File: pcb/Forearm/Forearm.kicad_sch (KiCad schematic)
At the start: 9 parts, among them J1 Conn_01x08_IMU_0, J2 Conn_01x16_Ribbon_To_Top, J3 Conn_01x16_Ribbon_To_Bottom, J4 Conn_01x03_DFR0205, U1 ESP32-S3-DEVKITC-1-N8R2

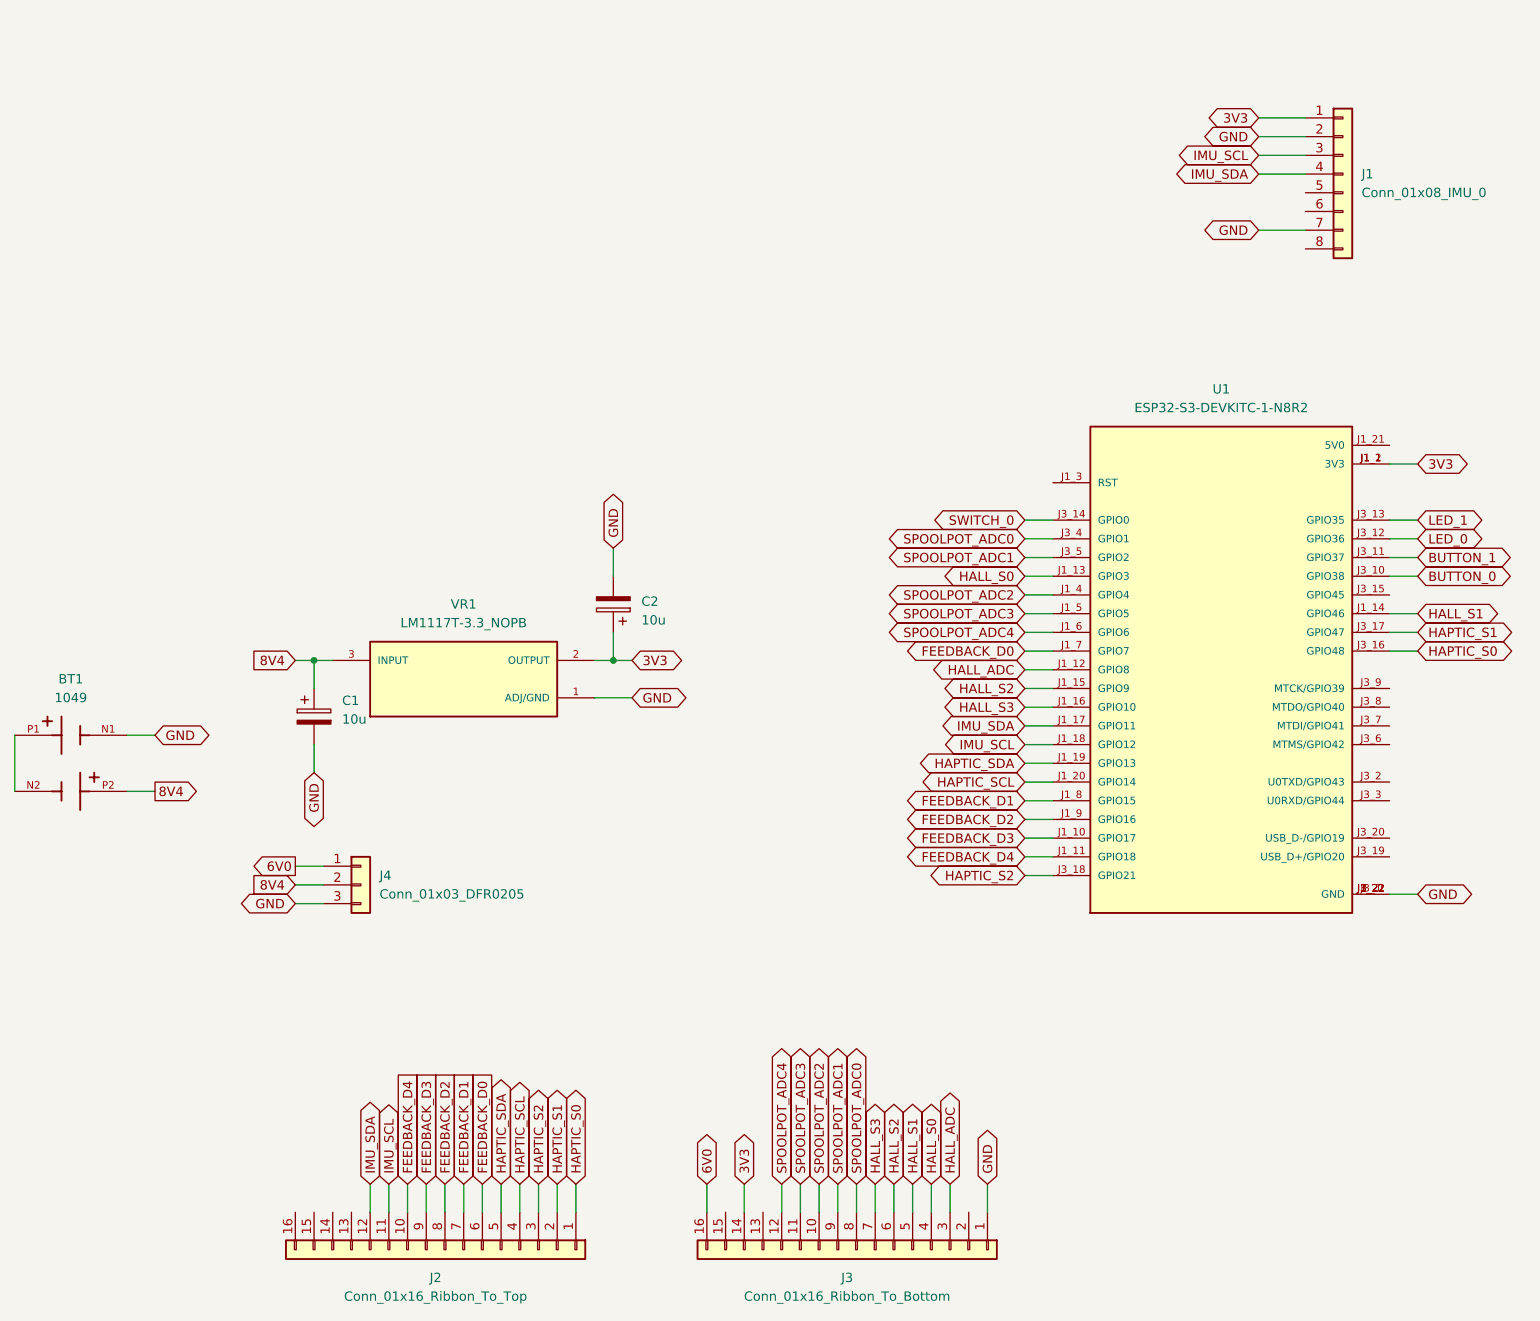
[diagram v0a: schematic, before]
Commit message: forward annotated schms to pcbs, added gnd and pwr planes, begun part placement
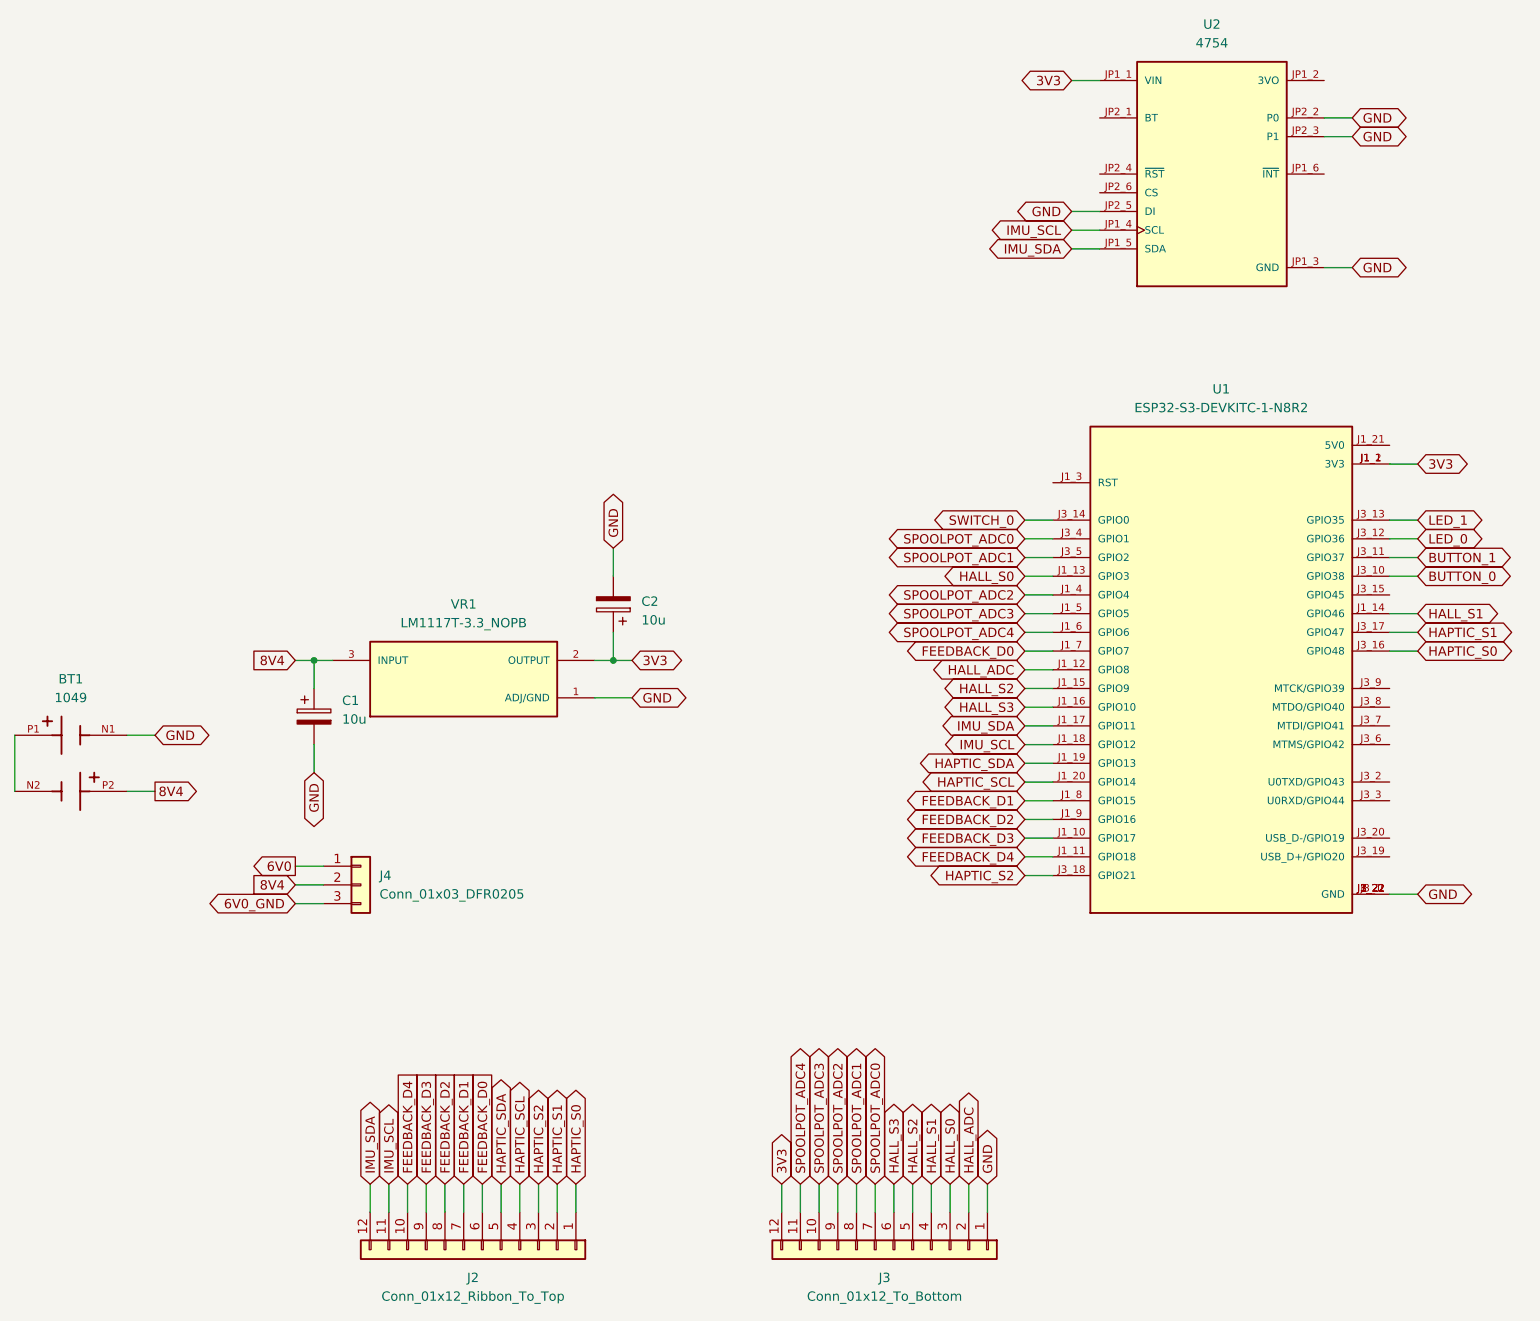
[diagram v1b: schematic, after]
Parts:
- removed J1: Conn_01x08_IMU_0, symbol Connector_Generic:Conn_01x08
- removed J2: Conn_01x16_Ribbon_To_Top, symbol Connector_Generic:Conn_01x16
- removed J3: Conn_01x16_Ribbon_To_Bottom, symbol Connector_Generic:Conn_01x16
- added J2: Conn_01x12_Ribbon_To_Top, 0522071233:0522071233, symbol Connector_Generic:Conn_01x12
- added J3: Conn_01x12_To_Bottom, 0522071233:0522071233, symbol Connector_Generic:Conn_01x12
- added U2: 4754, BNO085:MODULE_4754, symbol BNO085:4754
- C1, C2: footprint (none) -> Capacitor_THT:CP_Radial_Tantal_D6.0mm_P2.50mm
- J4: footprint (none) -> DFR0205:DFR0205
- VR1: footprint LM1117T-3.3_NOPB:TO254P1054X470X1955-3 -> LM1117T-3.3:LM1117T-3.3_NOPB
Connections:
- net 3V3: now also J3.12 (Pin_12), U2.JP1_1 (VIN)
- net FEEDBACK_D0: now also J2.6 (Pin_6)
- net FEEDBACK_D1: now also J2.7 (Pin_7)
- net FEEDBACK_D2: now also J2.8 (Pin_8)
- net FEEDBACK_D3: now also J2.9 (Pin_9)
- net FEEDBACK_D4: now also J2.10 (Pin_10)
- net GND: now also J3.1 (Pin_1), U2.JP1_3 (GND), U2.JP2_2 (P0), U2.JP2_3 (P1), U2.JP2_5 (DI); no longer J4.3 (Pin_3)
- net HALL_ADC: now also J3.2 (Pin_2)
- net HALL_S0: now also J3.3 (Pin_3)
- net HALL_S1: now also J3.4 (Pin_4)
- net HALL_S2: now also J3.5 (Pin_5)
- net HALL_S3: now also J3.6 (Pin_6)
- net HAPTIC_S0: now also J2.1 (Pin_1)
- net HAPTIC_S1: now also J2.2 (Pin_2)
- net HAPTIC_S2: now also J2.3 (Pin_3)
- net HAPTIC_SCL: now also J2.4 (Pin_4)
- net HAPTIC_SDA: now also J2.5 (Pin_5)
- net IMU_SCL: now also J2.11 (Pin_11), U2.JP1_4 (SCL)
- net IMU_SDA: now also J2.12 (Pin_12), U2.JP1_5 (SDA)
- net SPOOLPOT_ADC0: now also J3.7 (Pin_7)
- net SPOOLPOT_ADC1: now also J3.8 (Pin_8)
- net SPOOLPOT_ADC2: now also J3.9 (Pin_9)
- net SPOOLPOT_ADC3: now also J3.10 (Pin_10)
- net SPOOLPOT_ADC4: now also J3.11 (Pin_11)
- new net 6V0_GND: J4.3 (Pin_3)

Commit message: revised hand and made pass at routing forearm pcb
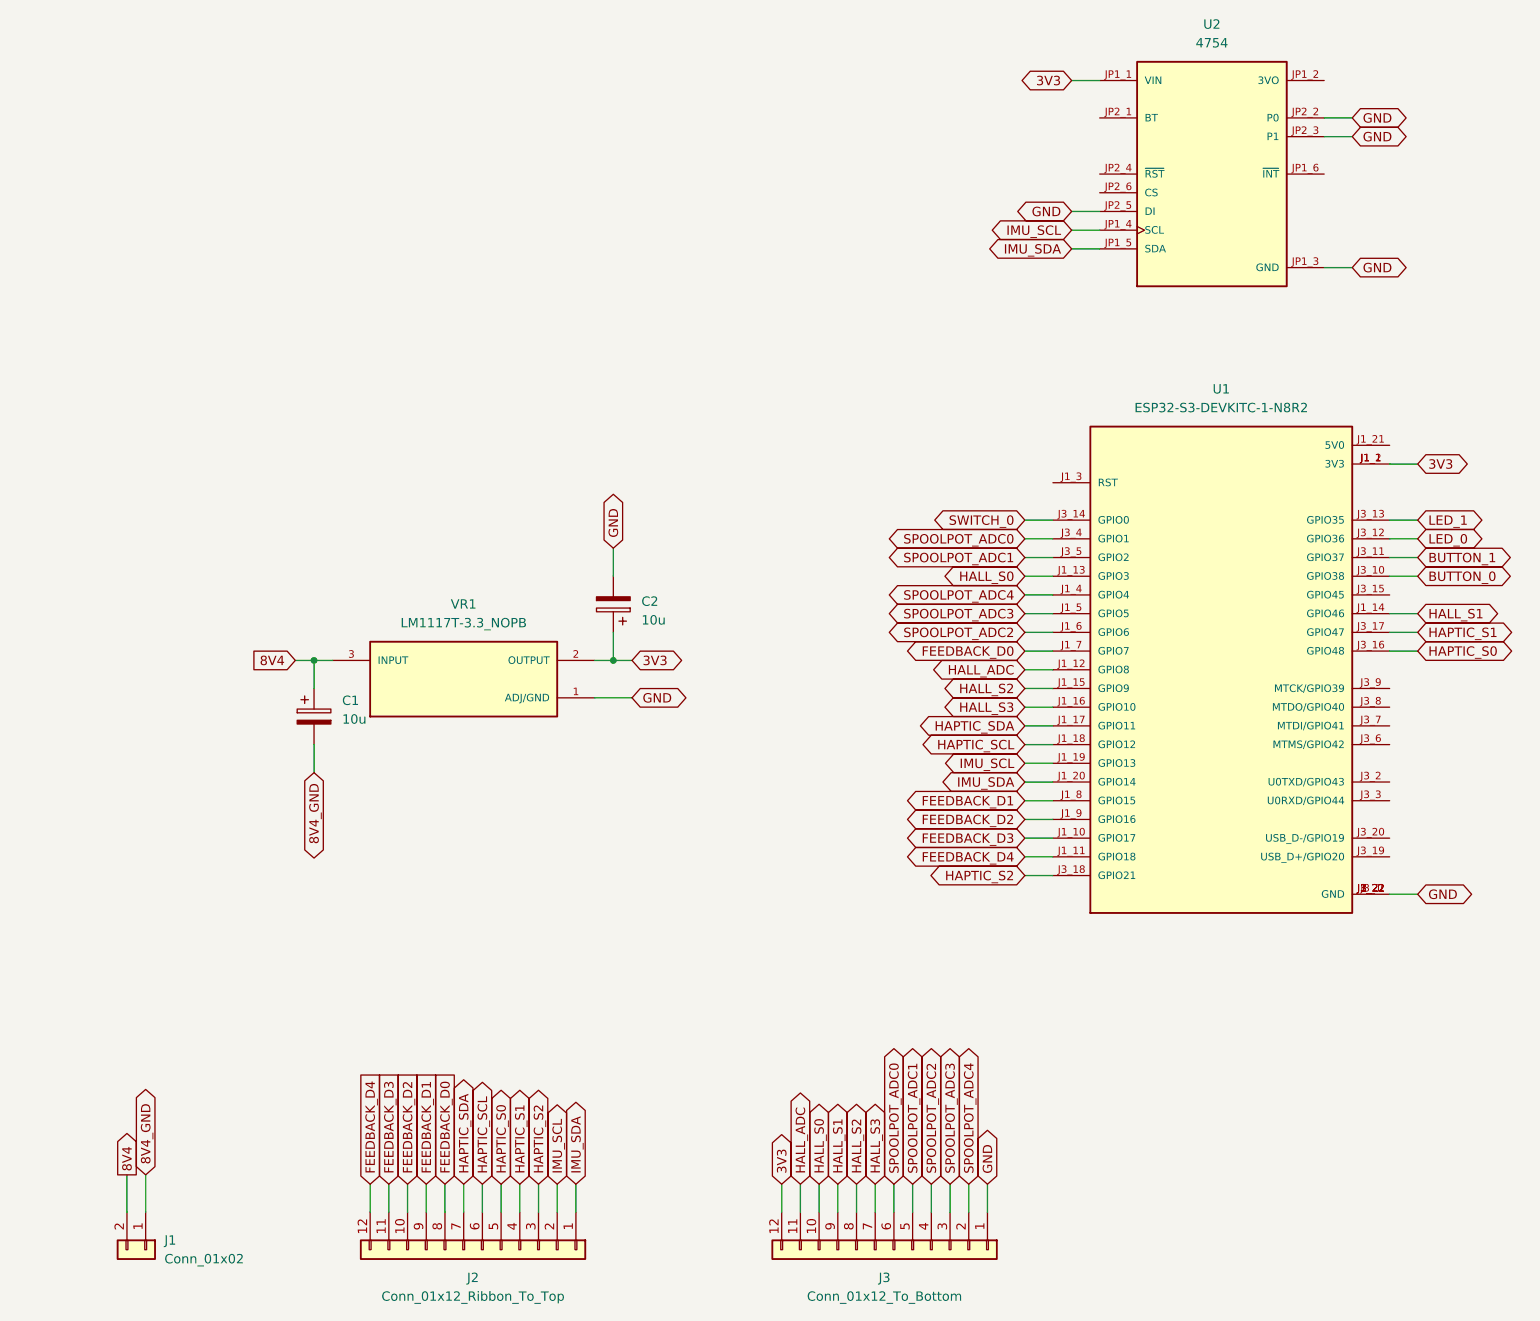
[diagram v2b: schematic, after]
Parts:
- removed BT1: 1049, 1049:BAT_1049, symbol 1049:1049
- removed J4: Conn_01x03_DFR0205, DFR0205:DFR0205, symbol Connector_Generic:Conn_01x03
- added J1: Conn_01x02, Connector_PinSocket_2.54mm:PinSocket_1x02_P2.54mm_Vertical, symbol Connector_Generic:Conn_01x02
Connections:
- net 8V4: now also J1.2 (Pin_2)
- net FEEDBACK_D0: now also J2.8 (Pin_8); no longer J2.6 (Pin_6)
- net FEEDBACK_D1: now also J2.9 (Pin_9); no longer J2.7 (Pin_7)
- net FEEDBACK_D2: now also J2.10 (Pin_10); no longer J2.8 (Pin_8)
- net FEEDBACK_D3: now also J2.11 (Pin_11); no longer J2.9 (Pin_9)
- net FEEDBACK_D4: now also J2.12 (Pin_12); no longer J2.10 (Pin_10)
- net GND: no longer C1.2
- net HALL_ADC: now also J3.11 (Pin_11); no longer J3.2 (Pin_2)
- net HALL_S0: now also J3.10 (Pin_10); no longer J3.3 (Pin_3)
- net HALL_S1: now also J3.9 (Pin_9); no longer J3.4 (Pin_4)
- net HALL_S2: now also J3.8 (Pin_8); no longer J3.5 (Pin_5)
- net HALL_S3: now also J3.7 (Pin_7); no longer J3.6 (Pin_6)
- net HAPTIC_S0: now also J2.5 (Pin_5); no longer J2.1 (Pin_1)
- net HAPTIC_S1: now also J2.4 (Pin_4); no longer J2.2 (Pin_2)
- net HAPTIC_SCL: now also J2.6 (Pin_6), U1.J1_18 (GPIO12); no longer J2.4 (Pin_4), U1.J1_20 (GPIO14)
- net HAPTIC_SDA: now also J2.7 (Pin_7), U1.J1_17 (GPIO11); no longer J2.5 (Pin_5), U1.J1_19 (GPIO13)
- net IMU_SCL: now also J2.2 (Pin_2), U1.J1_19 (GPIO13); no longer J2.11 (Pin_11), U1.J1_18 (GPIO12)
- net IMU_SDA: now also J2.1 (Pin_1), U1.J1_20 (GPIO14); no longer J2.12 (Pin_12), U1.J1_17 (GPIO11)
- net SPOOLPOT_ADC0: now also J3.6 (Pin_6); no longer J3.7 (Pin_7)
- net SPOOLPOT_ADC1: now also J3.5 (Pin_5); no longer J3.8 (Pin_8)
- net SPOOLPOT_ADC2: now also J3.4 (Pin_4), U1.J1_6 (GPIO6); no longer J3.9 (Pin_9), U1.J1_4 (GPIO4)
- net SPOOLPOT_ADC3: now also J3.3 (Pin_3); no longer J3.10 (Pin_10)
- net SPOOLPOT_ADC4: now also J3.2 (Pin_2), U1.J1_4 (GPIO4); no longer J3.11 (Pin_11), U1.J1_6 (GPIO6)
- new net 8V4_GND: C1.2, J1.1 (Pin_1)

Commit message: re-did layout of forearm board
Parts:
- C1, C2: footprint Capacitor_THT:CP_Radial_Tantal_D6.0mm_P2.50mm -> Capacitor_SMD:C_1206_3216Metric
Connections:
- net 8V4_GND is gone; now on net GND: C1.2, J1.1 (Pin_1)
- net HALL_ADC: now also U1.J1_16 (GPIO10); no longer U1.J1_12 (GPIO8)
- net HALL_S0: now also U1.J1_15 (GPIO9); no longer U1.J1_13 (GPIO3)
- net HALL_S2: now also U1.J1_13 (GPIO3); no longer U1.J1_15 (GPIO9)
- net HALL_S3: now also U1.J1_12 (GPIO8); no longer U1.J1_16 (GPIO10)
- net SPOOLPOT_ADC2: now also U1.J1_4 (GPIO4); no longer U1.J1_6 (GPIO6)
- net SPOOLPOT_ADC4: now also U1.J1_6 (GPIO6); no longer U1.J1_4 (GPIO4)
